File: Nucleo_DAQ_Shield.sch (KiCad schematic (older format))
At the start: 30 parts, among them J1 CONN_01X06, J2 CONN_01X06, J3 CONN_01X02, J4 CONN_01X02, J5 CONN_01X02, J6 CONN_COAXIAL, U1 4050, U10 ST_Nucleo144_F746ZG_CN10, U2 TL072, U3 7805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

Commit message: Reorganized schematic
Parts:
- C4, C5: footprint (none) -> Capacitors_SMD:C_0603
- D2: footprint (none) -> LEDs:LED_D5.0mm
- J1, J2: footprint (none) -> Pin_Headers:Pin_Header_Straight_1x06_Pitch2.54mm
- J3, J4, J5: footprint (none) -> Pin_Headers:Pin_Header_Straight_1x02_Pitch2.54mm
- JP1, JP2: footprint (none) -> Pin_Headers:Pin_Header_Straight_1x03_Pitch2.54mm
- R1, R2, R3: footprint (none) -> Resistors_SMD:R_0805
- U10: footprint (none) -> Pin_Headers:Pin_Header_Straight_2x17_Pitch2.54mm
- U2: footprint (none) -> Housings_SOIC:SOIC-8_3.9x4.9mm_Pitch1.27mm
- U3: footprint (none) -> TO_SOT_Packages_THT:TO-220_Vertical
- U7: footprint (none) -> Pin_Headers:Pin_Header_Straight_2x10_Pitch2.54mm
- U8: footprint (none) -> Pin_Headers:Pin_Header_Straight_2x08_Pitch2.54mm
- U9: footprint (none) -> Pin_Headers:Pin_Header_Straight_2x15_Pitch2.54mm
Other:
- note added: "Voltage Regulation"
- moved on the sheet: C1, C2, C3, C4, D2, J3, R2, U10, U4, U7, U8, U9

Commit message: Associated all footprints in CvPCB
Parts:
- C6: footprint (none) -> Capacitors_SMD:CP_Elec_6.3x5.8
- D1: footprint (none) -> Diodes_SMD:D_SOD-123
- J6: footprint (none) -> custom:SMA_uxcell
- JP3: footprint (none) -> Pin_Headers:Pin_Header_Straight_1x02_Pitch2.54mm
- JP4: footprint (none) -> Pin_Headers:Pin_Header_Straight_1x03_Pitch2.54mm
- U1: footprint (none) -> Housings_SOIC:SOIC-16_3.9x9.9mm_Pitch1.27mm
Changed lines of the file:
@@
 F 0 "U1" H 2345 4115 50  0000 C CNN
 F 1 "4050" H 2340 3875 50  0000 C CNN
-F 2 "" H 2150 4000 60  0001 C CNN
+F 2 "Housings_SOIC:SOIC-16_3.9x9.9mm_Pitch1.27mm" H 2150 4000 60  0001 C CNN
 F 3 "" H 2150 4000 60  0001 C CNN
 	2    2150 4000
@@
 F 0 "U1" H 2345 4515 50  0000 C CNN
 F 1 "4050" H 2340 4275 50  0000 C CNN
-F 2 "" H 2150 4400 60  0001 C CNN
+F 2 "Housings_SOIC:SOIC-16_3.9x9.9mm_Pitch1.27mm" H 2150 4400 60  0001 C CNN
 F 3 "" H 2150 4400 60  0001 C CNN
 	3    2150 4400
@@
 F 0 "U1" H 2345 4915 50  0000 C CNN
 F 1 "4050" H 2340 4675 50  0000 C CNN
-F 2 "" H 2150 4800 60  0001 C CNN
+F 2 "Housings_SOIC:SOIC-16_3.9x9.9mm_Pitch1.27mm" H 2150 4800 60  0001 C CNN
 F 3 "" H 2150 4800 60  0001 C CNN
 	4    2150 4800
@@
 F 0 "J6" H 4060 7120 50  0000 C CNN
 F 1 "CONN_COAXIAL" V 4165 7000 50  0000 C CNN
-F 2 "" H 4050 7000 50  0001 C CNN
+F 2 "custom:SMA_uxcell" H 4050 7000 50  0001 C CNN
 F 3 "" H 4050 7000 50  0001 C CNN
 	1    4050 7000
@@
 F 0 "D1" H 4700 6850 50  0000 C CNN
 F 1 "D_Schottky" H 4700 6650 50  0000 C CNN
-F 2 "" H 4700 6750 50  0001 C CNN
+F 2 "Diodes_SMD:D_SOD-123" H 4700 6750 50  0001 C CNN
 F 3 "" H 4700 6750 50  0001 C CNN
 	1    4700 6750
@@
 F 0 "JP3" H 5000 6680 50  0000 C CNN
 F 1 "ENVLP_OVP" H 5010 6540 50  0000 C CNN
-F 2 "" H 5000 6600 50  0001 C CNN
+F 2 "Pin_Headers:Pin_Header_Straight_1x02_Pitch2.54mm" H 5000 6600 50  0001 C CNN
 F 3 "" H 5000 6600 50  0001 C CNN
 	1    5000 6600
@@
 F 0 "U1" H 4245 2815 50  0000 C CNN
 F 1 "4050" H 4240 2575 50  0000 C CNN
-F 2 "" H 4050 2700 60  0001 C CNN
+F 2 "Housings_SOIC:SOIC-16_3.9x9.9mm_Pitch1.27mm" H 4050 2700 60  0001 C CNN
 F 3 "" H 4050 2700 60  0001 C CNN
 	5    4050 2700
@@
 F 0 "JP4" H 5100 4250 50  0000 L CNN
 F 1 "Jumper_NC_Dual" H 5050 4450 50  0000 C BNN
-F 2 "" H 5050 4350 50  0001 C CNN
+F 2 "Pin_Headers:Pin_Header_Straight_1x03_Pitch2.54mm" H 5050 4350 50  0001 C CNN
 F 3 "" H 5050 4350 50  0001 C CNN
 	1    5050 4350
@@
 F 0 "C6" H 7975 5750 50  0000 L CNN
 F 1 "22uF" H 7975 5550 50  0000 L CNN
-F 2 "" H 7988 5500 50  0001 C CNN
+F 2 "Capacitors_SMD:CP_Elec_6.3x5.8" H 7988 5500 50  0001 C CNN
 F 3 "" H 7950 5650 50  0001 C CNN
 	1    7950 5650
@@
 F 0 "U1" H 1795 5815 50  0000 C CNN
 F 1 "4050" H 1790 5575 50  0000 C CNN
-F 2 "" H 1600 5700 60  0001 C CNN
+F 2 "Housings_SOIC:SOIC-16_3.9x9.9mm_Pitch1.27mm" H 1600 5700 60  0001 C CNN
 F 3 "" H 1600 5700 60  0001 C CNN
 	1    1600 5700

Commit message: Aligned connectors to Arduino shield layout
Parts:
- removed U3: 7805, TO_SOT_Packages_THT:TO-220_Vertical, symbol 7805
- added U3: LM7805CT, TO_SOT_Packages_THT:TO-220_Vertical, symbol LM7805CT
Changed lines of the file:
@@
 $EndComp
 $Comp
-L 7805 U3
-U 1 1 595429B4
-P 3200 1050
-F 0 "U3" H 3350 854 50  0000 C CNN
-F 1 "7805" H 3200 1250 50  0000 C CNN
-F 2 "TO_SOT_Packages_THT:TO-220_Vertical" H 3200 1050 50  0001 C CNN
-F 3 "" H 3200 1050 50  0001 C CNN
-	1    3200 1050
-	1    0    0    -1
-$EndComp
-$Comp
 L GND #PWR01
 U 1 1 59542B17
@@
 Connection ~ 3800 1000
 Connection ~ 4300 1000
-Wire Wire Line
-	3600 1000 4900 1000
 Connection ~ 2600 1000
 Connection ~ 2100 1000
 Wire Wire Line
-	1900 1000 2800 1000
-Wire Wire Line
 	2200 2900 2600 2900
 Wire Wire Line
@@
 Text Notes 2600 600  0    60   ~ 0
 Voltage Regulation
+$Comp
+L LM7805CT U3
+U 1 1 5964BE4D
+P 3200 1050
+F 0 "U3" H 3000 1250 50  0000 C CNN
+F 1 "LM7805CT" H 3200 1250 50  0000 L CNN
+F 2 "TO_SOT_Packages_THT:TO-220_Vertical" H 3200 1150 50  0001 C CIN
+F 3 "" H 3200 1050 50  0001 C CNN
+	1    3200 1050
+	1    0    0    -1
+$EndComp
+Wire Wire Line
+	3600 1000 4900 1000
+Wire Wire Line
+	1900 1000 2800 1000
 $EndSCHEMATC

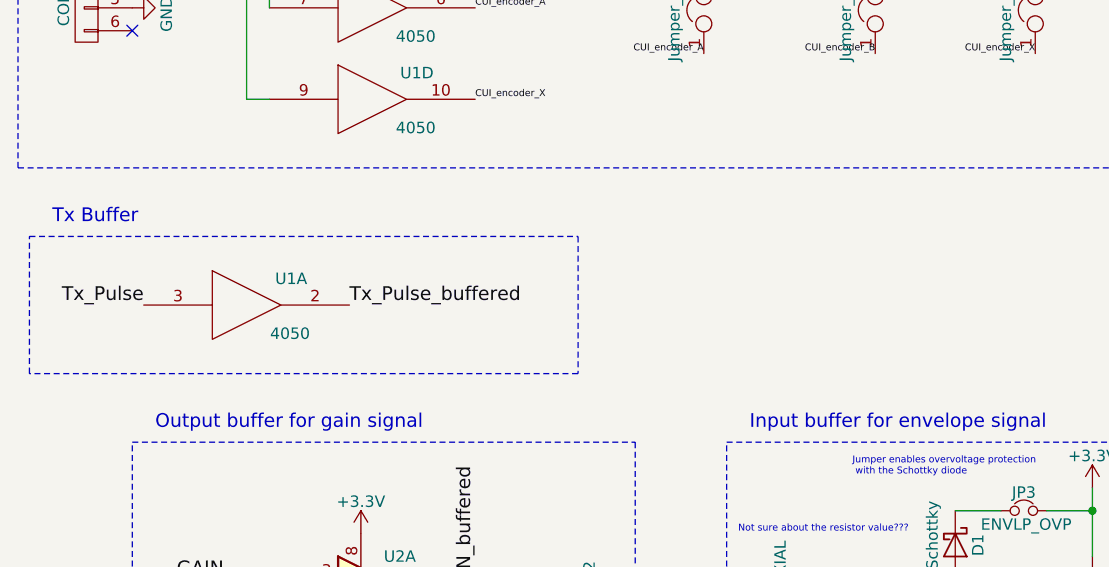
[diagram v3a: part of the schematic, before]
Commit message: Rough placement of all components
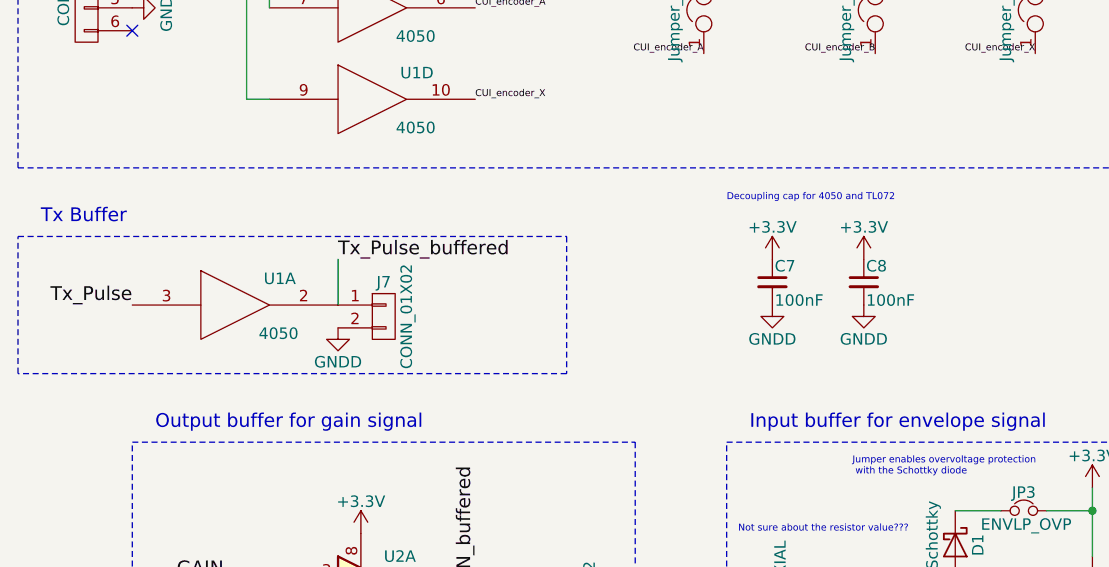
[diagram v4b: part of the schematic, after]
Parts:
- added C7, C8: 100nF, Capacitors_SMD:C_0603, symbol C_Small
- added J7: CONN_01X02, Pin_Headers:Pin_Header_Straight_1x02_Pitch2.54mm, symbol CONN_01X02
- C1: footprint Capacitors_Tantalum_SMD:CP_Tantalum_Case-A_EIA-3216-18_Hand -> Capacitors_Tantalum_SMD:CP_Tantalum_Case-A_EIA-3216-18_Reflow
- U3: footprint TO_SOT_Packages_THT:TO-220_Vertical -> TO_SOT_Packages_THT:TO-92_Inline_Narrow_Oval
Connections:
- net +3.3VA: now also C7.1, C8.1
- net GND: now also C7.2, C8.2, J7.2 (P2)
- net Tx_Pulse_buffered: now also J7.1 (P1)
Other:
- note added: "Decoupling cap for 4050 and TL072"
- moved on the sheet: U1A
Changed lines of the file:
@@
 F 0 "C1" H 2110 1170 50  0000 L CNN
 F 1 "10uF tant" H 2110 1020 50  0000 L CNN
-F 2 "Capacitors_Tantalum_SMD:CP_Tantalum_Case-A_EIA-3216-18_Hand" H 2100 1100 50  0001 C CNN
+F 2 "Capacitors_Tantalum_SMD:CP_Tantalum_Case-A_EIA-3216-18_Reflow" H 2100 1100 50  0001 C CNN
 F 3 "" H 2100 1100 50  0001 C CNN
 	1    2100 1100
@@
 L 4050 U1
 U 1 1 595E88D9
-P 1600 5700
-F 0 "U1" H 1795 5815 50  0000 C CNN
-F 1 "4050" H 1790 5575 50  0000 C CNN
-F 2 "Housings_SOIC:SOIC-16_3.9x9.9mm_Pitch1.27mm" H 1600 5700 60  0001 C CNN
-F 3 "" H 1600 5700 60  0001 C CNN
-	1    1600 5700
+P 1550 5700
+F 0 "U1" H 1745 5815 50  0000 C CNN
+F 1 "4050" H 1740 5575 50  0000 C CNN
+F 2 "Housings_SOIC:SOIC-16_3.9x9.9mm_Pitch1.27mm" H 1550 5700 60  0001 C CNN
+F 3 "" H 1550 5700 60  0001 C CNN
+	1    1550 5700
 	1    0    0    -1
 $EndComp
-Text Label 1150 5700 2    60   ~ 0
+Text Label 1100 5700 2    60   ~ 0
 Tx_Pulse
-Text Label 2050 5700 0    60   ~ 0
+Text Label 2000 5500 0    60   ~ 0
 Tx_Pulse_buffered
-Text Notes 750  5350 0    60   ~ 0
+Text Notes 700  5350 0    60   ~ 0
 Tx Buffer
 $Bitmap
@@
 $EndComp
 Wire Notes Line
-	650  6000 650  5400
+	600  6000 600  5400
 Wire Notes Line
-	3050 6000 650  6000
+	3000 6000 600  6000
 Wire Notes Line
-	3050 5400 3050 6000
+	3000 5400 3000 6000
 Wire Notes Line
-	650  5400 3050 5400
+	600  5400 3000 5400
 Wire Notes Line
 	5600 6200 5600 4400
@@
 F 0 "U3" H 3000 1250 50  0000 C CNN
 F 1 "LM7805CT" H 3200 1250 50  0000 L CNN
-F 2 "TO_SOT_Packages_THT:TO-220_Vertical" H 3200 1150 50  0001 C CIN
+F 2 "TO_SOT_Packages_THT:TO-92_Inline_Narrow_Oval" H 3200 1150 50  0001 C CIN
 F 3 "" H 3200 1050 50  0001 C CNN
 	1    3200 1050
@@
 Wire Wire Line
 	1900 1000 2800 1000
+$Comp
+L C_Small C7
+U 1 1 59640337
+P 3900 5600
+F 0 "C7" H 3910 5670 50  0000 L CNN
+F 1 "100nF" H 3910 5520 50  0000 L CNN
+F 2 "Capacitors_SMD:C_0603" H 3900 5600 50  0001 C CNN
+F 3 "" H 3900 5600 50  0001 C CNN
+	1    3900 5600
+	1    0    0    -1
+$EndComp
+$Comp
+L GNDD #PWR047
+U 1 1 59640585
+P 3900 5700
+F 0 "#PWR047" H 3900 5450 50  0001 C CNN
+F 1 "GNDD" H 3900 5550 50  0000 C CNN
+F 2 "" H 3900 5700 50  0001 C CNN
+F 3 "" H 3900 5700 50  0001 C CNN
+	1    3900 5700
+	1    0    0    -1
+$EndComp
+$Comp
+L +3.3V #PWR048
+U 1 1 596405FC
+P 3900 5500
+F 0 "#PWR048" H 3900 5350 50  0001 C CNN
+F 1 "+3.3V" H 3900 5640 50  0000 C CNN
+F 2 "" H 3900 5500 50  0001 C CNN
+F 3 "" H 3900 5500 50  0001 C CNN
+	1    3900 5500
+	1    0    0    -1
+$EndComp
+Text Notes 3700 5250 0    30   ~ 0
+Decoupling cap for 4050 and TL072
+$Comp
+L C_Small C8
+U 1 1 596410DD
+P 4300 5600
+F 0 "C8" H 4310 5670 50  0000 L CNN
+F 1 "100nF" H 4310 5520 50  0000 L CNN
+F 2 "Capacitors_SMD:C_0603" H 4300 5600 50  0001 C CNN
+F 3 "" H 4300 5600 50  0001 C CNN
+	1    4300 5600
+	1    0    0    -1
+$EndComp
+$Comp
+L GNDD #PWR049
+U 1 1 596410E3
+P 4300 5700
+F 0 "#PWR049" H 4300 5450 50  0001 C CNN
+F 1 "GNDD" H 4300 5550 50  0000 C CNN
+F 2 "" H 4300 5700 50  0001 C CNN
+F 3 "" H 4300 5700 50  0001 C CNN
+	1    4300 5700
+	1    0    0    -1
+$EndComp
+$Comp
+L +3.3V #PWR050
+U 1 1 596410E9
+P 4300 5500
+F 0 "#PWR050" H 4300 5350 50  0001 C CNN
+F 1 "+3.3V" H 4300 5640 50  0000 C CNN
+F 2 "" H 4300 5500 50  0001 C CNN
+F 3 "" H 4300 5500 50  0001 C CNN
+	1    4300 5500
+	1    0    0    -1
+$EndComp
+$Comp
+L CONN_01X02 J7
+U 1 1 59642310
+P 2200 5750
+F 0 "J7" H 2200 5900 50  0000 C CNN
+F 1 "CONN_01X02" V 2300 5750 50  0000 C CNN
+F 2 "Pin_Headers:Pin_Header_Straight_1x02_Pitch2.54mm" H 2200 5750 50  0001 C CNN
+F 3 "" H 2200 5750 50  0001 C CNN
+	1    2200 5750
+	1    0    0    -1
+$EndComp
+$Comp
+L GNDD #PWR051
+U 1 1 596424FC
+P 2000 5800
+F 0 "#PWR051" H 2000 5550 50  0001 C CNN
+F 1 "GNDD" H 2000 5650 50  0000 C CNN
+F 2 "" H 2000 5800 50  0001 C CNN
+F 3 "" H 2000 5800 50  0001 C CNN
+	1    2000 5800
+	1    0    0    -1
+$EndComp
+Wire Wire Line
+	2000 5500 2000 5700
 $EndSCHEMATC

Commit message: Mostly isolated AGND and DGND planes and fully routed analog portion; partially routed digital side
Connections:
- net 5V_CUI_B: now reaches J1.1 (P1), U1.5
- net 5V_CUI_A: now reaches J1.3 (P3), U1.7
- net 5V_CUI_X: now reaches J1.4 (P4), U1.9
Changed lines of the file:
@@
 	0    -1   -1   0
 $EndComp
+Text Label 1350 4000 0    30   ~ 0
+5V_CUI_B
+Text Label 1350 4200 0    30   ~ 0
+5V_CUI_A
+Text Label 1350 4300 0    30   ~ 0
+5V_CUI_X
 $EndSCHEMATC

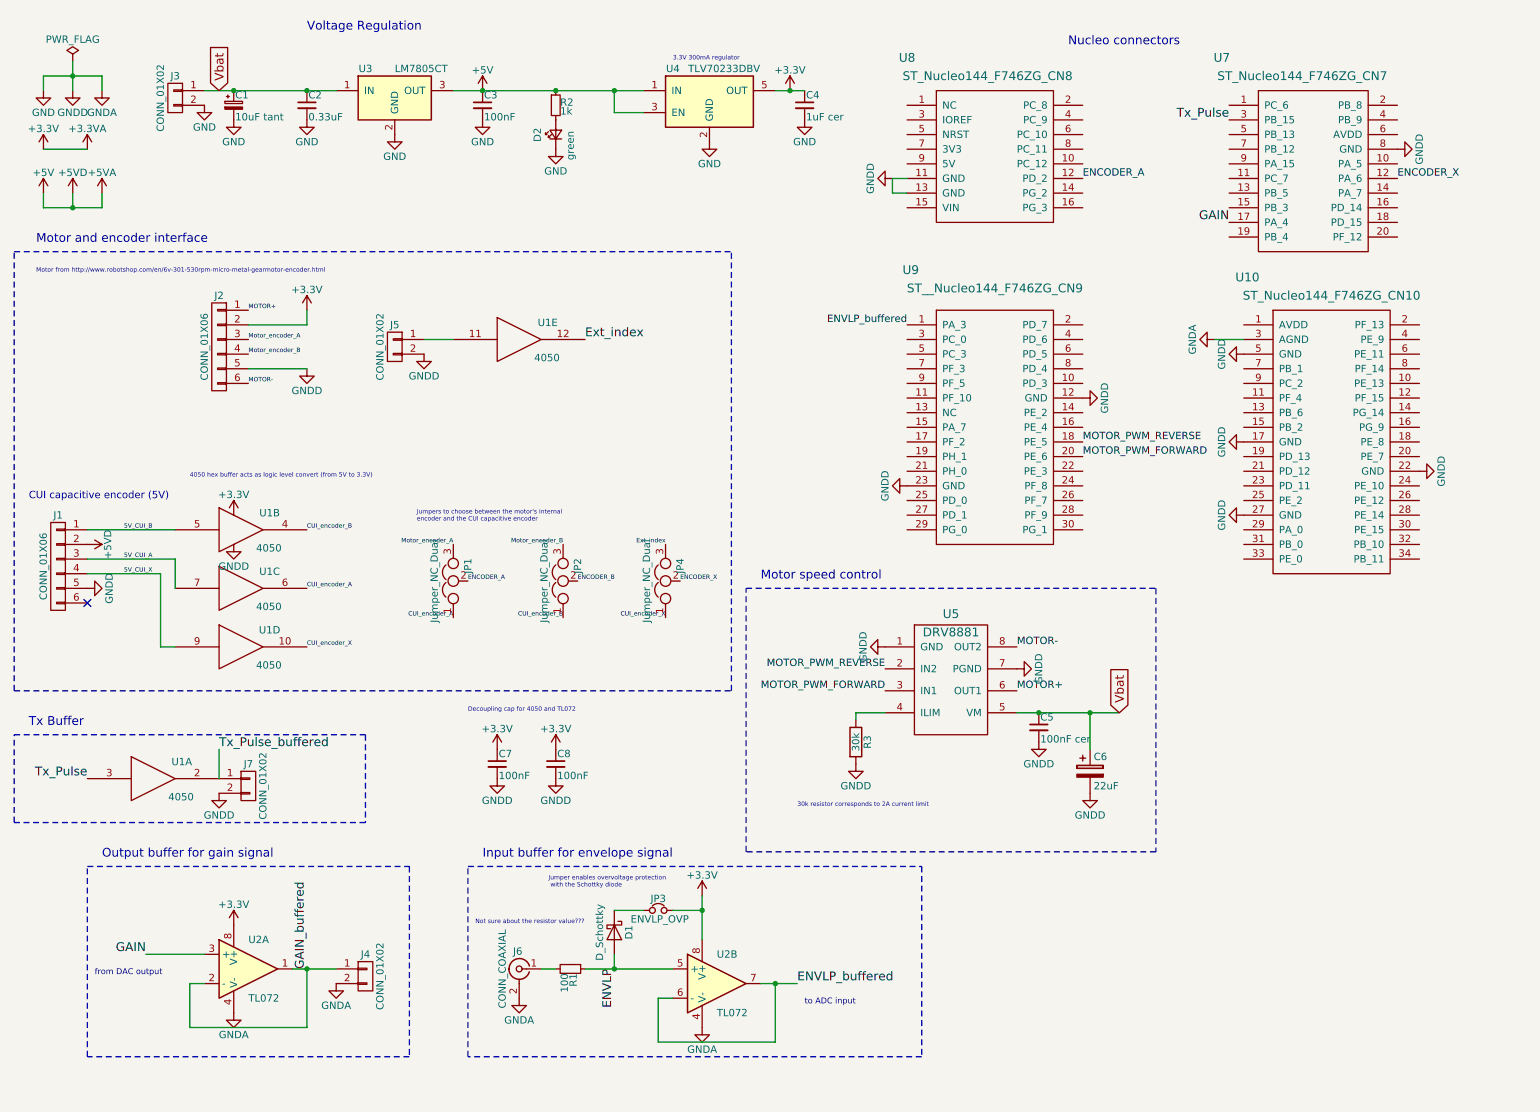
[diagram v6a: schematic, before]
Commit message: Removed extraneous parts and finished PCB layout
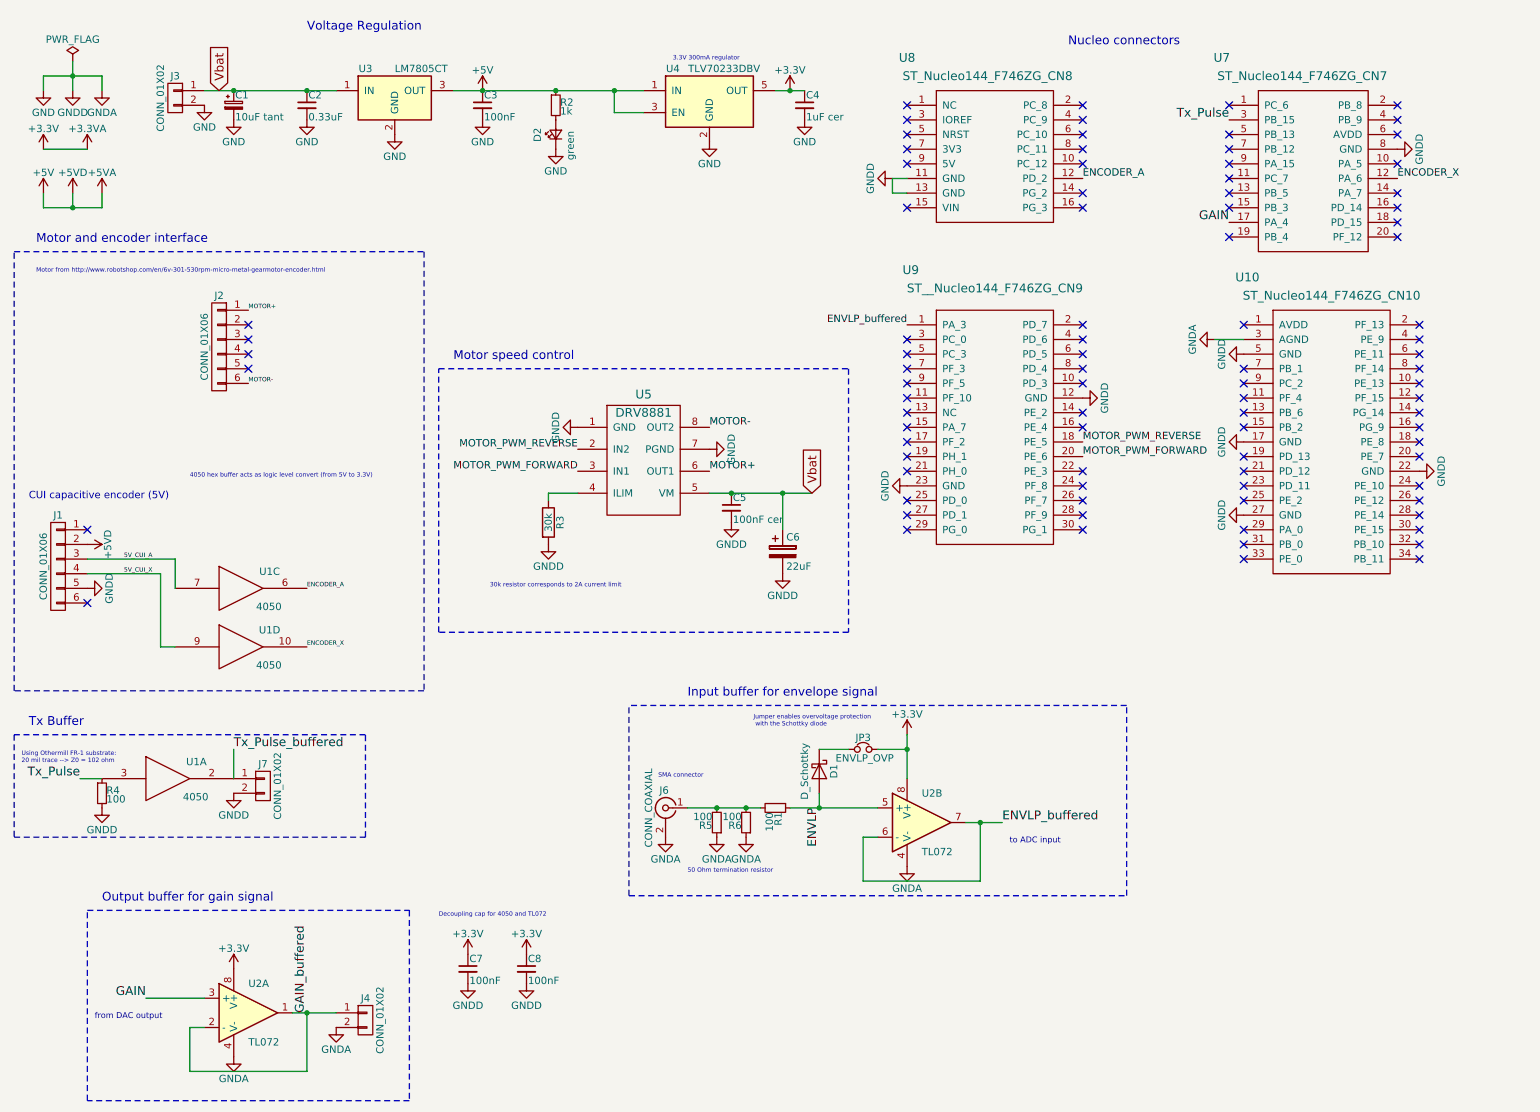
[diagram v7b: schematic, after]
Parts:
- removed J5: CONN_01X02, Pin_Headers:Pin_Header_Straight_1x02_Pitch2.54mm, symbol CONN_01X02
- removed JP1, JP2, JP4: Jumper_NC_Dual, Pin_Headers:Pin_Header_Straight_1x03_Pitch2.54mm, symbol Jumper_NC_Dual
- removed unit 2 of U1
- removed unit 5 of U1
- added R4, R5, R6: 100, Resistors_SMD:R_0805, symbol R_Small
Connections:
- net CUI_encoder_A is gone; now on net ENCODER_A: U1.6
- net CUI_encoder_X is gone; now on net ENCODER_X: U1.10
- net +3.3VA: no longer J2.2 (P2), U1.1 (VCC), U1.1 (VCC), U1.1 (VCC)
- net GND: now also R4.2, R5.1, R6.1; no longer J2.5 (P5), U1.8 (VSS), U1.8 (VSS), U1.8 (VSS)
- net Tx_Pulse: now also R4.1
- net at J6.1 (In), R1.2: now also R5.2, R6.2
- net 5V_CUI_B: no longer names the net of J1.1 (P1)
- net Motor_encoder_A: no longer names the net of J2.3 (P3)
- net Motor_encoder_B: no longer names the net of J2.4 (P4)
- new net VCC: U1.1 (VCC), U1.1 (VCC), U1.1 (VCC)
- new net VSS: U1.8 (VSS), U1.8 (VSS), U1.8 (VSS)
- no-connect marks 1 -> 89
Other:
- note added: "50 Ohm termination resistor"
- note added: "SMA connector"
- note added: "Using Othermill FR-1 substrate:\n20 mil trace --> Z0 = 102 ohm"
- note removed: "Jumpers to choose between the motor's internal \nencoder and the CUI capacitive encoder"
- note removed: "Not sure about the resistor value???"
- moved on the sheet: C5, C6, C7, C8, D1, J4, J6, J7, JP3, R1, R3, U1A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
